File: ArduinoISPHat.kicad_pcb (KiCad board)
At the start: 2 copper layers, 54.6 x 56.5 mm, 20 parts, among them J1 Conn_01x02, J2 Conn_01x06, J7 D7, SW1 SW_DPDT_x2, U1 ATmega328P-PU, Y1 Crystal

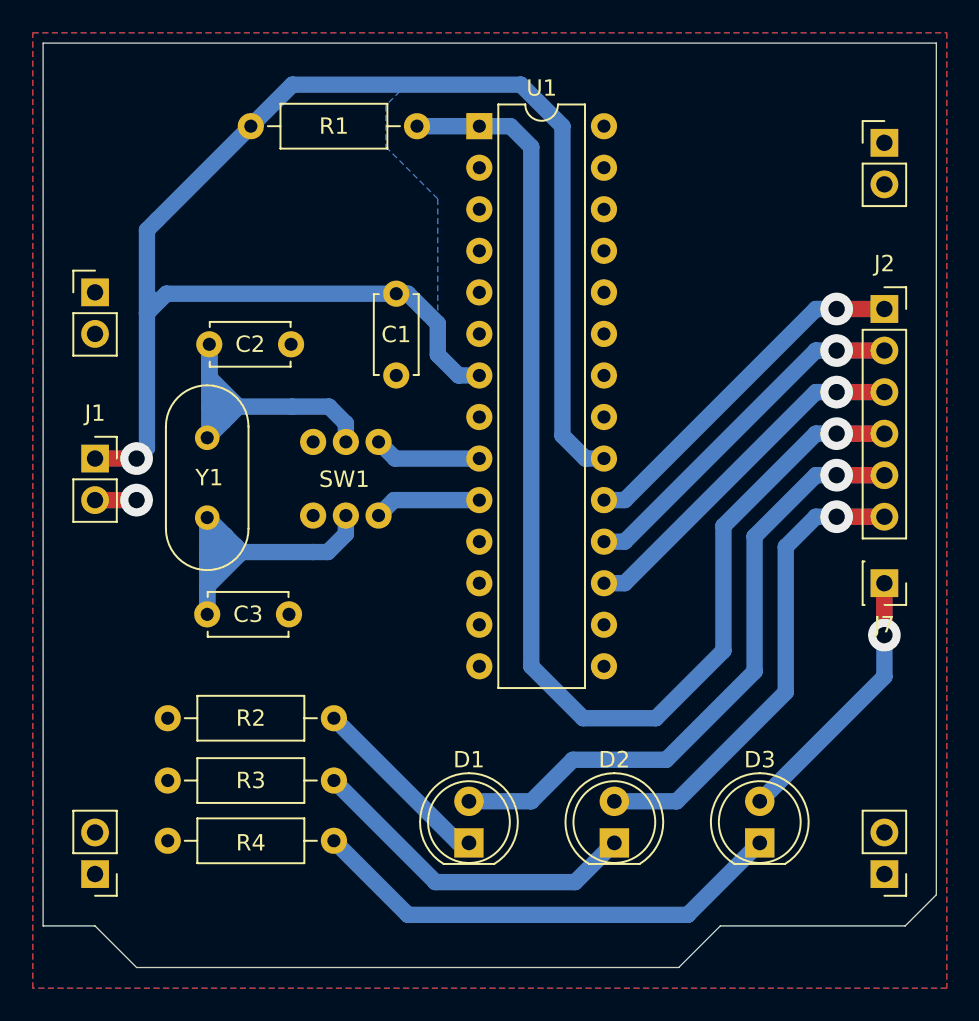
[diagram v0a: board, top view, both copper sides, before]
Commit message: Updated layout
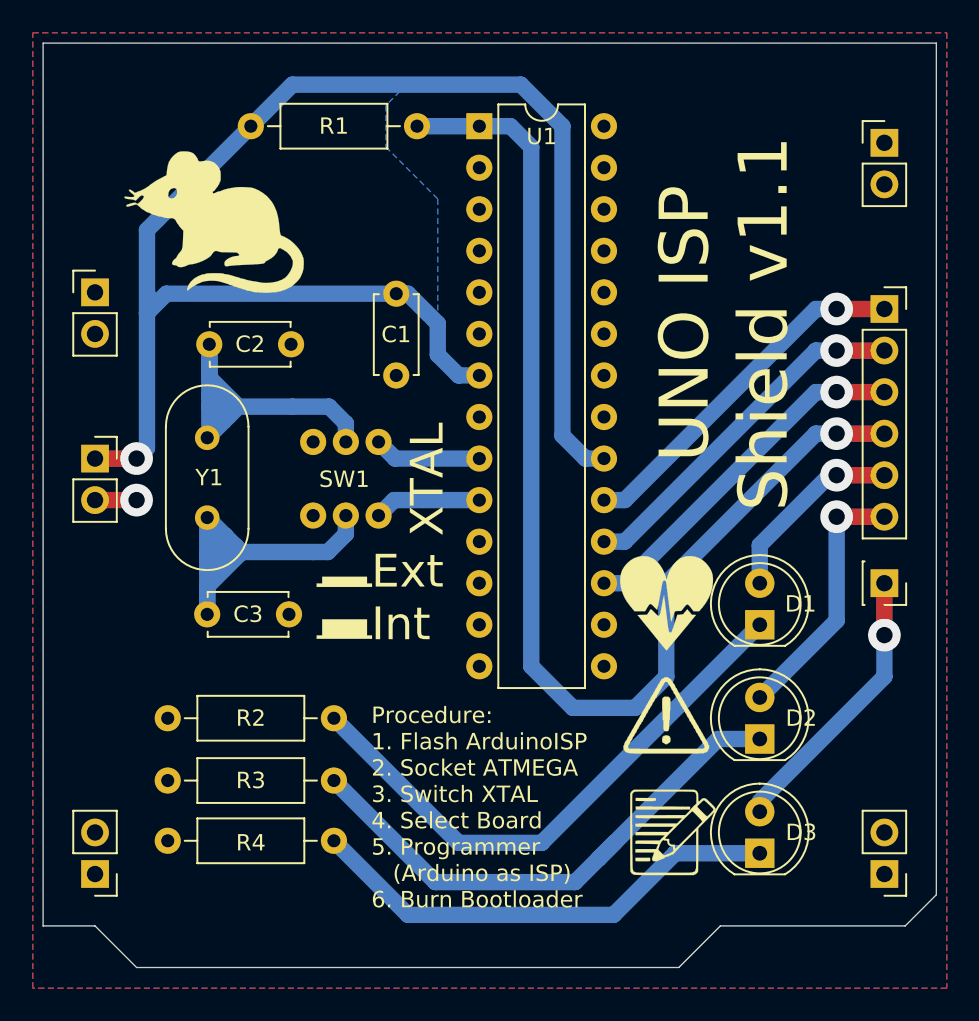
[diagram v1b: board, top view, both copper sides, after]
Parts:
- added G***: LOGO, logos:Mouse, F.Cu at (23.9, 41.8)
- added G***: LOGO, logos:ButtonIn, F.Cu at (31.8, 64.0)
- added G***: LOGO, logos:ButtonOut, F.Cu at (31.8, 67.2)
- added G***: LOGO, logos:Alert, F.Cu at (51.4, 72.6)
- added G***: LOGO, logos:Write, F.Cu at (51.7, 79.9)
- added G***: LOGO, logos:HeartBeat, F.Cu at (51.4, 66.0)
- added REF**: OSHW-Symbol_8.9x8mm_SilkScreen, Symbol:OSHW-Symbol_8.9x8mm_SilkScreen, B.Cu at (28.4, 42.7)
- moved D1 22.2 mm to (57.1, 67.3)
- moved D2 10.9 mm to (57.1, 74.3)
- moved D3 0.64 mm to (57.1, 81.3)
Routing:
- net D9: track 38.5 -> 11.7 mm
- net Net-(D1-Pad1): track 11.4 -> 34.7 mm
- net D8: track 28.9 -> 15.9 mm
- net Net-(D2-Pad1): track 20.7 -> 33.6 mm
- net D10: track 73.8 -> 72.2 mm
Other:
- rule pad_to_mask_clearance: 0.05 -> 0
- board text added: "Ext Int"
- board text added: "JCLCJLCJL"
- board text added: "Procedure: 1. Flash ArduinoISP 2. Socket ATMEGA 3. Switch XTAL 4. Select Board 5. Programmer (Arduino as ISP) 6. Burn Bootloader"
- board text added: "SFA 2021"
- board text added: "UNO ISP Shield v1.1"
- board text added: "XTAL"
